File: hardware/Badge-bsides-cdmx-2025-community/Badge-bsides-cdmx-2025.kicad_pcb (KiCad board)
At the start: 2 copper layers, 50 x 110 mm, 30 parts, among them J1 SWDIO, J3 ADDON, J4 Conn_01x04_Pin, J5 I2C, J6 Conn_01x04_Pin, P6 USB_C_Plug_USB2.0, Q3 DMG3415U-7, SW11 ON, SW2 RESET, U1 PY32F030F28U6TR, U6 AP2112K-3.3

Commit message: feat(Hw):started_routing
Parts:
- added C67: 10uF, Capacitor_SMD:C_0603_1608Metric, B.Cu at (-10.3, 13.9)
- added C68: 10uF, Capacitor_SMD:C_0603_1608Metric, B.Cu at (-24.3, 33.3)
- added C69: 10uF, Capacitor_SMD:C_0603_1608Metric, B.Cu at (-39.1, 13.9)
- added C70: 10uF, Capacitor_SMD:C_0603_1608Metric, B.Cu at (-39.7, 34.8)
- added R5: 10k, Resistor_SMD:R_0603_1608Metric, B.Cu at (-10.3, 15.4)
- added R6: 10k, Resistor_SMD:R_0603_1608Metric, B.Cu at (-24.3, 34.8)
- added R7: 10k, Resistor_SMD:R_0603_1608Metric, B.Cu at (-39.1, 15.4)
- added R8: 10k, Resistor_SMD:R_0603_1608Metric, B.Cu at (-39.7, 33.3)
- added SW10: SW_Push, Footprints:TS1088R02026, F.Cu at (-39.6, 34.0)
- added SW7: SW_Push, Footprints:TS1088R02026, F.Cu at (-39.1, 14.5)
- added SW8: SW_Push, Footprints:TS1088R02026, F.Cu at (-10.3, 14.5)
- added SW9: SW_Push, Footprints:TS1088R02026, F.Cu at (-24.2, 34.0)
- added kibuzzard-6841C014: G***, kibuzzard-6841C014, B.Cu at (-23.0, 89.0)
- BT3, BT4: moved to B.Cu
- J3: moved to F.Cu
- J4: footprint Connector_PinHeader_2.54mm:PinHeader_1x04_P2.54mm_Vertical -> Connector_PinHeader_2.54mm:PinHeader_1x04_P2.54mm_Horizontal; moved to B.Cu
- J6: footprint Connector_PinHeader_2.54mm:PinHeader_1x04_P2.54mm_Vertical -> Connector_PinSocket_2.54mm:PinSocket_1x04_P2.54mm_Horizontal; moved to B.Cu
- moved J1 222.0 mm to (-46.9, 44.6)
- moved J3 189.9 mm to (-43.8, 6.31), turned to 90 degrees
- moved D10 187.9 mm to (-39.4, 59.9)
- moved R11 187.0 mm to (-38.9, 62.6)
- moved C33 179.6 mm to (-11.9, 65.6)
- moved F3 179.2 mm to (-11.9, 68.6)
- moved D4 179.0 mm to (-41.7, 71.9)
- moved P6 179.0 mm to (-6.55, 71.0)
- moved Q3 179.0 mm to (-41.2, 76.1)
- moved R10 179.0 mm to (-44.0, 76.1)
- moved SW11 179.0 mm to (-46.3, 70.5)
- moved U1 179.0 mm to (-25.2, 52.7)
- moved J4 179.0 mm to (-4.38, 58.2)
- moved C10 178.9 mm to (-37.0, 69.5)
- moved C26 178.9 mm to (-32.8, 68.0)
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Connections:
- BT3 pad 2: +3.3V -> +BATT
- J3 pad 5: /GPIO1 -> /GPIO2
- J3 pad 6: /GPIO2 -> /GPIO1
- J4 pad 1: /RX -> GND
- J4 pad 2: /RX -> GND
- J4 pad 3: GND -> /RX
- J4 pad 4: GND -> /RX
- J6 pad 1: /TX -> GND
- J6 pad 2: /TX -> GND
- J6 pad 3: GND -> /TX
- J6 pad 4: GND -> /TX
- U1 pad 1: unconnected-(U1-PA5-Pad1) -> /BTTN2
- U1 pad 10: unconnected-(U1-PB6-Pad10) -> /LED1
- U1 pad 16: /GPIO2 -> /BTTN4
- U1 pad 17: /GPIO1 -> /BTTN3
- U1 pad 2: /LED1 -> /BTTN1
- U1 pad 20: unconnected-(U1-PA4-Pad20) -> /LED2
- U1 pad 3: /LED2 -> /GPIO1
- U1 pad 5: unconnected-(U1-PA12-Pad5) -> /GPIO2
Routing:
- net /BTTN1: track 0.00 -> 57.5 mm, vias 0 -> 1
- net Net-(BT3--): track 0.00 -> 55.1 mm
- net /BTTN3: track 0.00 -> 49.9 mm, vias 0 -> 1
- net VBUS: track 0.00 -> 40.2 mm, vias 0 -> 2
- net /BTTN2: track 0.00 -> 32.3 mm, vias 0 -> 2
- net /BTTN4: track 0.00 -> 31.3 mm, vias 0 -> 1
- net +BATT: track 0.00 -> 16.9 mm
- net Net-(SW11-A): track 0.00 -> 14.8 mm
- net Net-(F3-Pad1): track 0.00 -> 10.8 mm
- net Net-(D4-K): track 0.00 -> 9.51 mm
- net /TX: track 0.00 -> 8.26 mm, vias 0 -> 1
- net Net-(P6-CC): track 0.00 -> 7.73 mm
- net Net-(P6-VCONN): track 0.00 -> 6.86 mm
- net /SDA: track 0.00 -> 6.40 mm, vias 0 -> 1
- net +3V3: track 0.00 -> 1.80 mm
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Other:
- board size 50 x 110 mm -> 50.1 x 110 mm

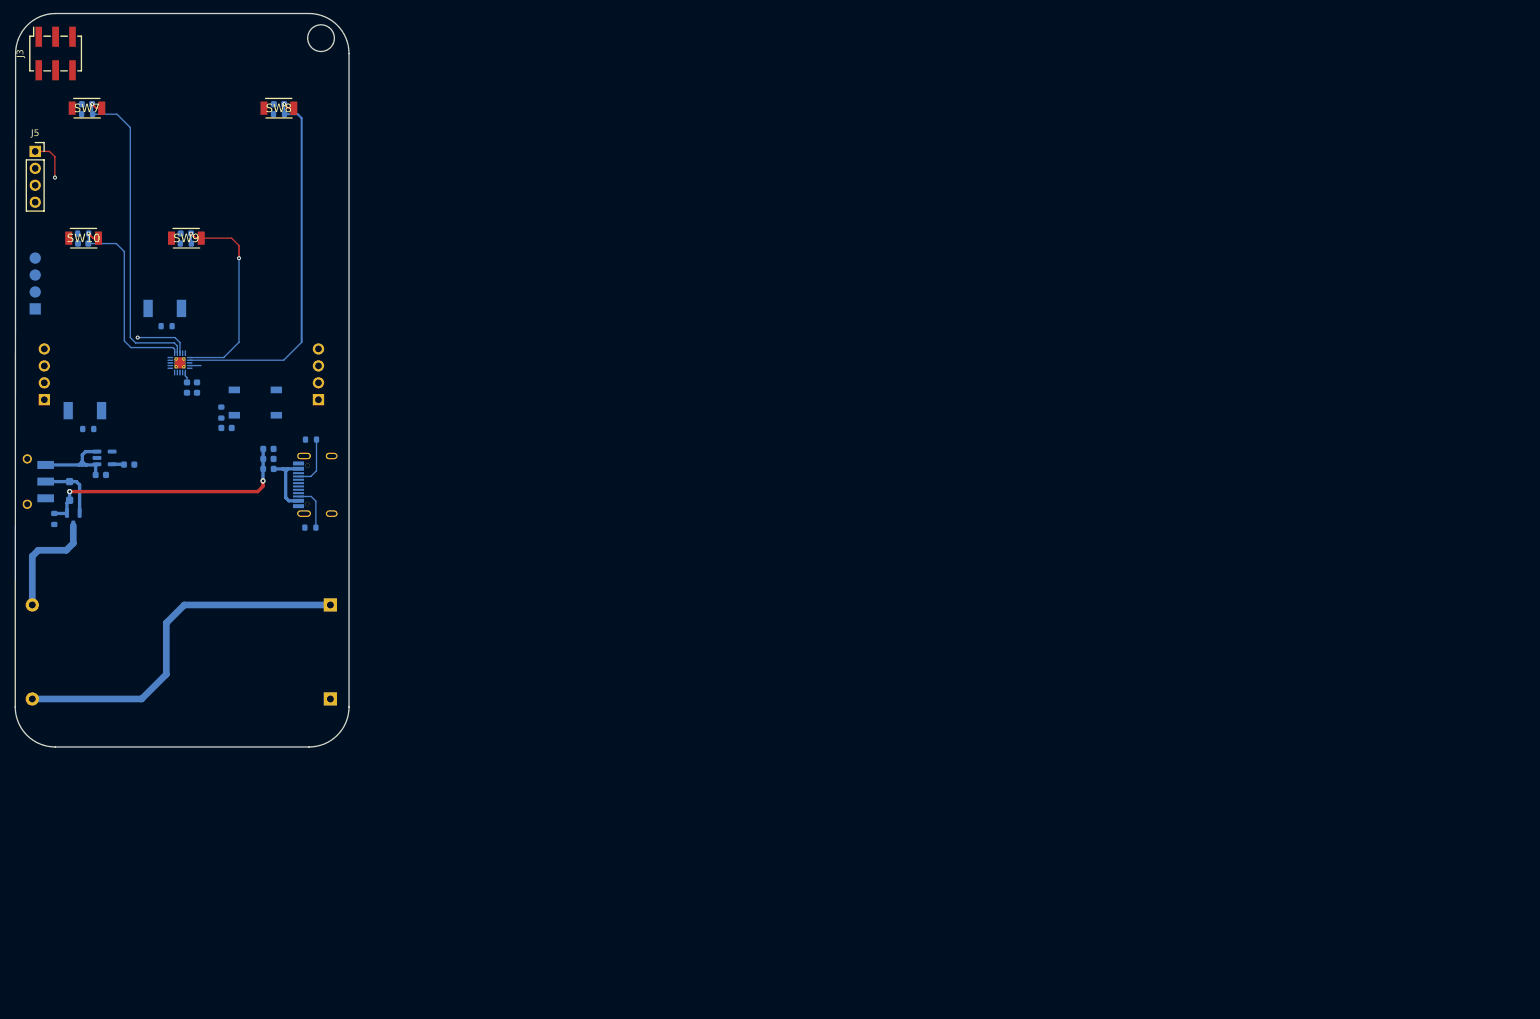
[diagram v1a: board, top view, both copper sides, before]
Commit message: feat(Hw):Route_Community
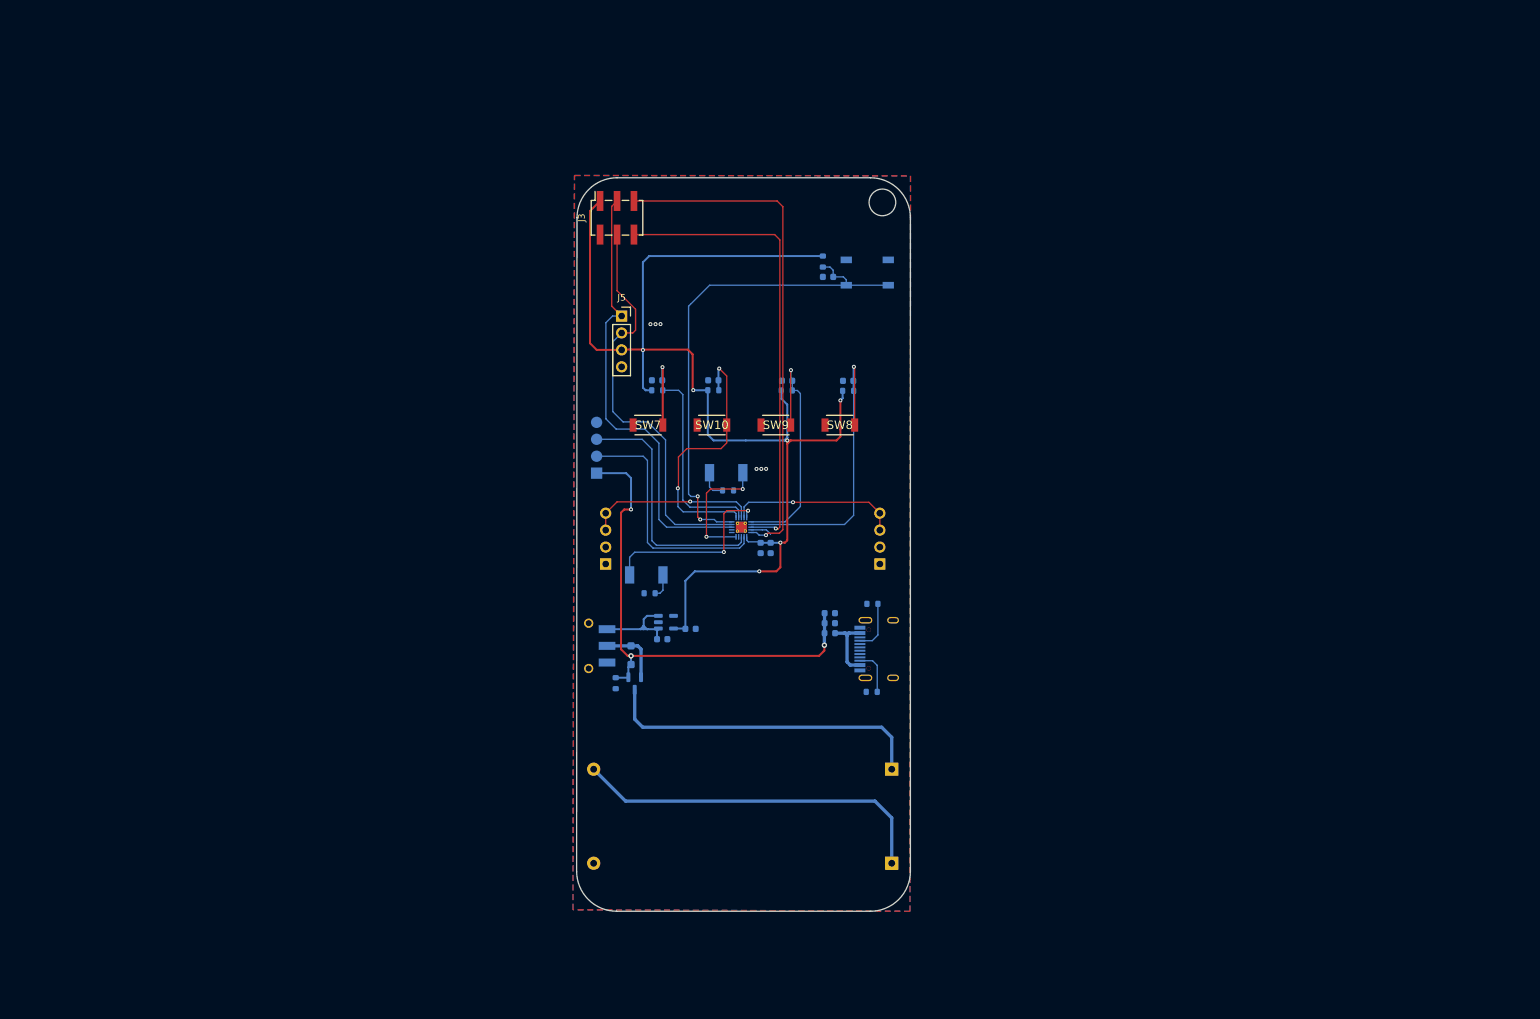
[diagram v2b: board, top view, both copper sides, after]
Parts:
- moved SW10 98.3 mm to (54.6, 62.0)
- moved R8 97.4 mm to (54.8, 56.8)
- moved C70 96.7 mm to (54.8, 55.3)
- moved SW7 96.6 mm to (45.0, 62.0)
- moved SW8 96.6 mm to (73.8, 62.0)
- moved C69 95.0 mm to (46.4, 55.3)
- moved R7 95.0 mm to (46.4, 56.8)
- moved C67 94.9 mm to (75.1, 55.4)
- moved R5 94.9 mm to (75.1, 56.9)
- moved SW2 93.8 mm to (77.9, 39.2)
- moved C6 93.0 mm to (72.0, 39.8)
- moved R4 93.0 mm to (71.3, 37.5), turned to 90 degrees
- moved C68 92.8 mm to (65.9, 55.4)
- moved R6 92.8 mm to (65.9, 56.8)
- moved SW9 92.7 mm to (64.2, 62.0)
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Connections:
- BT3 pad 1: Net-(BT3--) -> +BATT
- BT3 pad 2: +BATT -> Net-(BT3--)
- BT4 pad 1: GND -> Net-(BT3--)
- BT4 pad 2: Net-(BT3--) -> GND
- C26 pad 1: +3V3 -> +3.3V
- J3 pad 1: +3V3 -> +3.3V
- R4 pad 2: +3V3 -> +3.3V
- R5 pad 2: +3V3 -> +3.3V
- R6 pad 2: +3V3 -> +3.3V
- R7 pad 2: +3V3 -> +3.3V
- R8 pad 2: +3V3 -> +3.3V
- U6 pad 5: +3V3 -> +3.3V
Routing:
- net +3.3V: track 1.65 -> 186.5 mm, vias 0 -> 6
- net /GPIO2: track 0.00 -> 76.4 mm, vias 0 -> 1
- net /NTST: track 0.00 -> 75.2 mm, vias 0 -> 2
- net /GPIO1: track 0.00 -> 69.9 mm, vias 0 -> 1
- net /SCL: track 0.03 -> 61.5 mm
- net /SDA: track 6.40 -> 67.7 mm, vias 1 -> 0
- net /SWCLK: track 0.00 -> 37.3 mm
- net /SWDIO: track 0.00 -> 36.3 mm
- net VBUS: track 40.2 -> 74.5 mm, vias 2 -> 3
- net +BATT: track 16.9 -> 48.9 mm
- net /LED2: track 0.00 -> 27.8 mm, vias 0 -> 2
- net /RX: track 0.00 -> 25.5 mm, vias 0 -> 1
- net /LED1: track 0.00 -> 19.1 mm, vias 0 -> 2
- net /TX: track 8.26 -> 25.5 mm
- net /BTTN1: track 57.5 -> 47.1 mm
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- added copper zone on B.Cu, net GND
- added copper zone on F.Cu, net GND

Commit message: feat(Hw):Neopixels_added(sponsor)
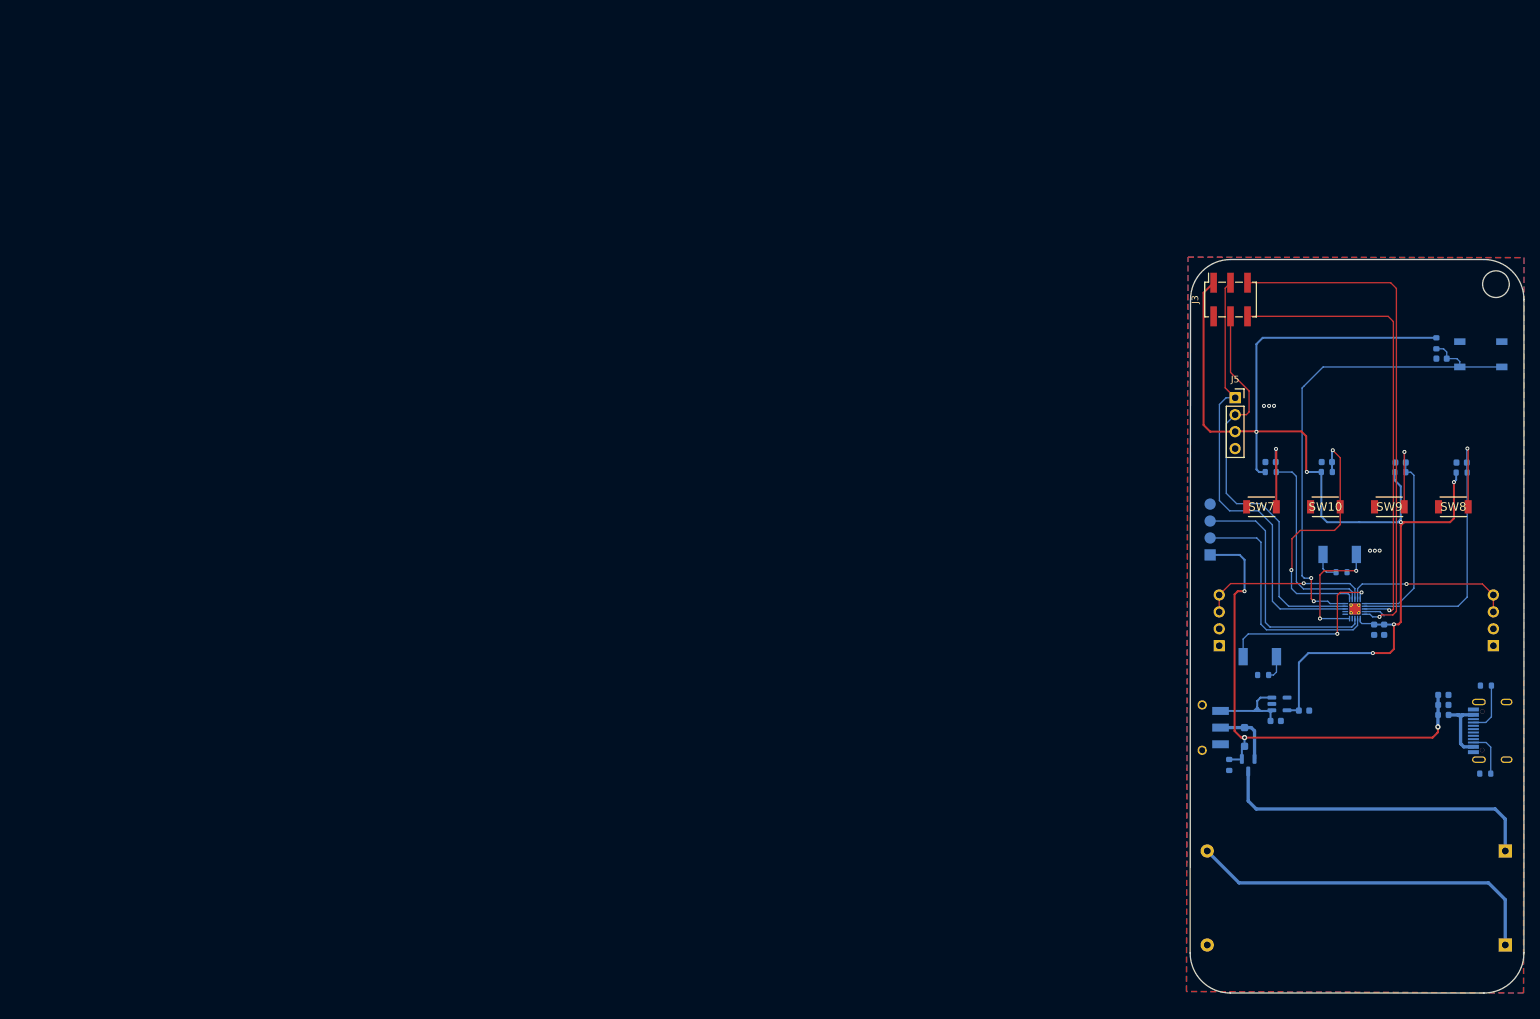
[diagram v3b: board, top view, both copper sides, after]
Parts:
- added kibuzzard-6841DE4B: G***, kibuzzard-6841DE4B, B.Cu at (128.2, 101.8)
- added kibuzzard-6841DE57: G***, kibuzzard-6841DE57, B.Cu at (128.2, 113.0)
- added kibuzzard-6841DE72: G***, kibuzzard-6841DE72, B.Cu at (169.9, 55.3)
- added kibuzzard-6841DE7C: G***, kibuzzard-6841DE7C, B.Cu at (133.6, 91.3)
- added kibuzzard-6841DE87: G***, kibuzzard-6841DE87, B.Cu at (169.1, 91.5)
- moved C10 92.8 mm to (139.2, 106.4)
- moved C26 92.8 mm to (143.4, 104.8)
- moved D9 92.8 mm to (148.8, 81.4)
- moved Q3 92.8 mm to (135.1, 113.0)
- moved R9 92.8 mm to (149.1, 84.1)
- moved SW7 92.8 mm to (137.0, 74.3)
- moved U1 92.8 mm to (151.1, 89.6)
- moved U6 92.8 mm to (139.7, 103.8)
- moved C27 92.8 mm to (164.3, 104.0)
- moved C33 92.8 mm to (164.3, 102.5)
- moved C6 92.8 mm to (164.0, 52.1)
- moved F3 92.8 mm to (164.3, 105.5)
- moved J3 92.8 mm to (132.4, 43.2)
- moved J6 92.8 mm to (130.7, 95.1)
- moved P6 92.8 mm to (169.7, 107.9)
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
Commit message: feat(Hw):Community_Badge_Added_Neopixels
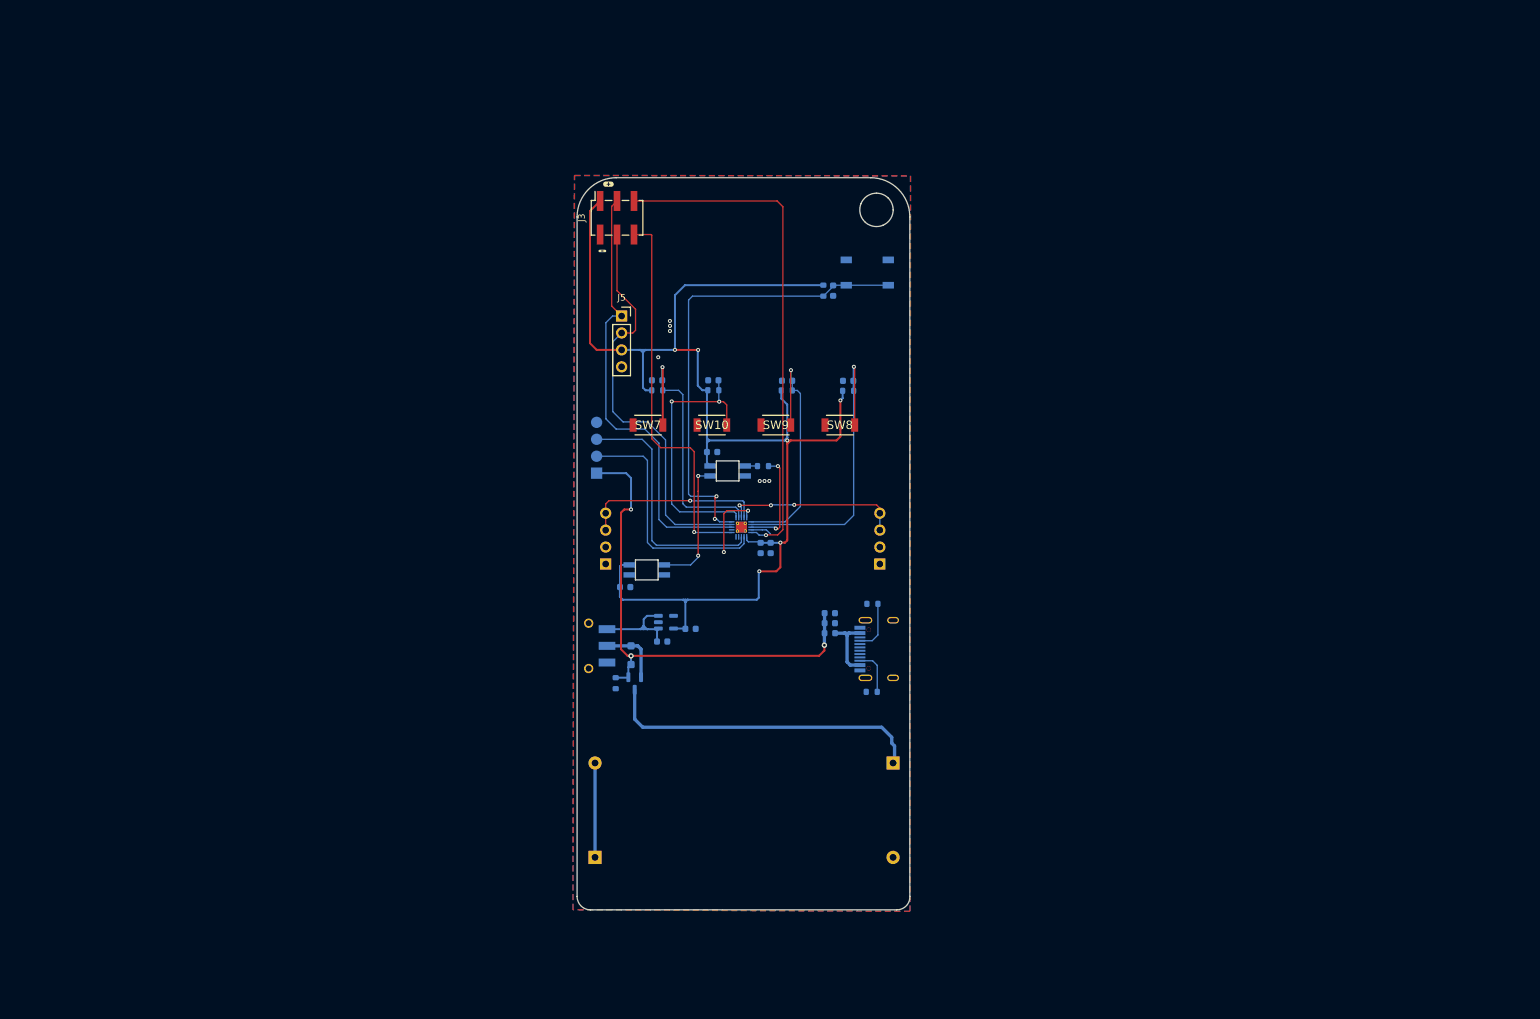
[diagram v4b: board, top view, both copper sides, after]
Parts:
- removed D10, D9: R_LED, Footprints:LYT77K-K2M1
- removed R11, R9: 220, Resistor_SMD:R_0603_1608Metric
- removed kibuzzard-6841C014: G***, kibuzzard-6841C014
- removed kibuzzard-6841DE4B: G***, kibuzzard-6841DE4B
- removed kibuzzard-6841DE57: G***, kibuzzard-6841DE57
- removed kibuzzard-6841DE72: G***, kibuzzard-6841DE72
- removed kibuzzard-6841DE7C: G***, kibuzzard-6841DE7C
- removed kibuzzard-6841DE87: G***, kibuzzard-6841DE87
- added C29: 100nF, Capacitor_SMD:C_0603_1608Metric, B.Cu at (54.6, 66.1)
- added C30: 100nF, Capacitor_SMD:C_0603_1608Metric, B.Cu at (41.6, 86.3)
- added D19: WS2812B, Footprints:LED_SK6812-E, B.Cu at (57.0, 68.9)
- added D20: WS2812B, Footprints:LED_SK6812-E, B.Cu at (44.9, 83.8)
- added R3: 1K, Resistor_SMD:R_0603_1608Metric, B.Cu at (62.3, 68.2)
- added kibuzzard-68434005: G***, kibuzzard-68434005, B.Cu at (79.7, 85.4)
- added kibuzzard-68434035: G***, kibuzzard-68434035, B.Cu at (38.3, 85.5)
- added kibuzzard-68434047: G***, kibuzzard-68434047, B.Cu at (37.0, 89.8)
- added kibuzzard-68434058: G***, kibuzzard-68434058, B.Cu at (36.3, 100.5)
- added kibuzzard-68434071: G***, kibuzzard-68434071, B.Cu at (78.0, 34.7)
- added kibuzzard-68434153: G***, kibuzzard-68434153, F.Cu at (39.1, 25.9)
- added kibuzzard-68434168: G***, kibuzzard-68434168, F.Cu at (38.2, 35.9)
- added kibuzzard-6843433E: G***, kibuzzard-6843433E, B.Cu at (61.2, 113.6)
- moved BT4 137.1 mm to (37.1, 126.9), turned to 0 degrees
- moved C26 92.8 mm to (51.4, 92.6)
- moved Q3 92.8 mm to (43.0, 100.8)
- moved SW7 92.8 mm to (45.0, 62.0)
- moved U1 92.8 mm to (59.0, 77.3)
- moved U6 92.8 mm to (47.7, 91.6)
- moved C27 92.8 mm to (72.3, 91.7)
- moved C33 92.8 mm to (72.3, 90.2)
- moved F3 92.8 mm to (72.3, 93.2)
- moved J3 92.8 mm to (40.4, 30.9)
- moved J6 92.8 mm to (38.7, 82.9)
- moved P6 92.8 mm to (77.6, 95.6)
- moved R6 92.8 mm to (65.9, 56.8)
- moved SW11 92.8 mm to (37.9, 95.1)
- moved C28 92.8 mm to (63.4, 80.5)
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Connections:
- J4 pad 3: /RX -> /TX
- J4 pad 4: /RX -> /TX
- J6 pad 3: /TX -> /RX
- J6 pad 4: /TX -> /RX
- U1 pad 11: unconnected-(U1-PB7-Pad11) -> /GPIO1
- U1 pad 3: /GPIO1 -> /NEO
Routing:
- net Net-(BT3--): track 54.5 -> 14.2 mm
- net Net-(D19-DOUT): track 0.00 -> 19.6 mm, vias 0 -> 2
- net /LED1: track 19.1 -> 0.00 mm, vias 2 -> 0
- net /LED2: track 27.8 -> 10.7 mm
- net +3.3V: track 186.5 -> 201.9 mm
- net /NEO: track 0.00 -> 15.3 mm, vias 0 -> 2
- net /GPIO1: track 69.9 -> 58.1 mm
- net /NTST: track 75.2 -> 70.6 mm
- net Net-(D9-K): track 4.32 -> 0.00 mm
- net Net-(D10-K): track 3.66 -> 0.00 mm
- net Net-(D19-DIN): track 0.00 -> 1.88 mm
- net /RX: track 25.5 -> 27.3 mm
- net /TX: track 25.5 -> 26.5 mm, vias 1 -> 3
- net /BTTN4: track 40.3 -> 41.0 mm
- net +BATT: track 48.9 -> 48.2 mm
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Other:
- board size 50.1 x 110 mm -> 49.9 x 109.8 mm
